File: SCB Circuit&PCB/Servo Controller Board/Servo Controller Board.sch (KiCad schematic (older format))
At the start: 2 parts

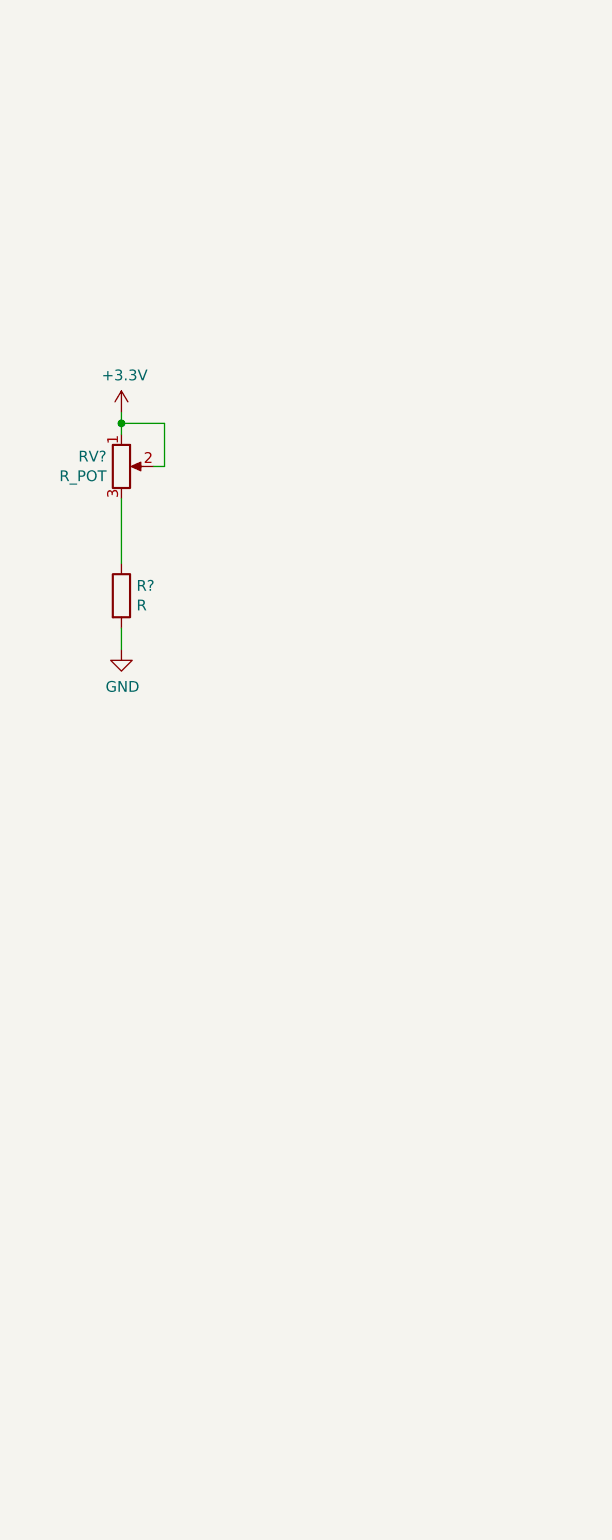
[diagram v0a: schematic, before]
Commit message: Added external interrupt for timer enable/disable
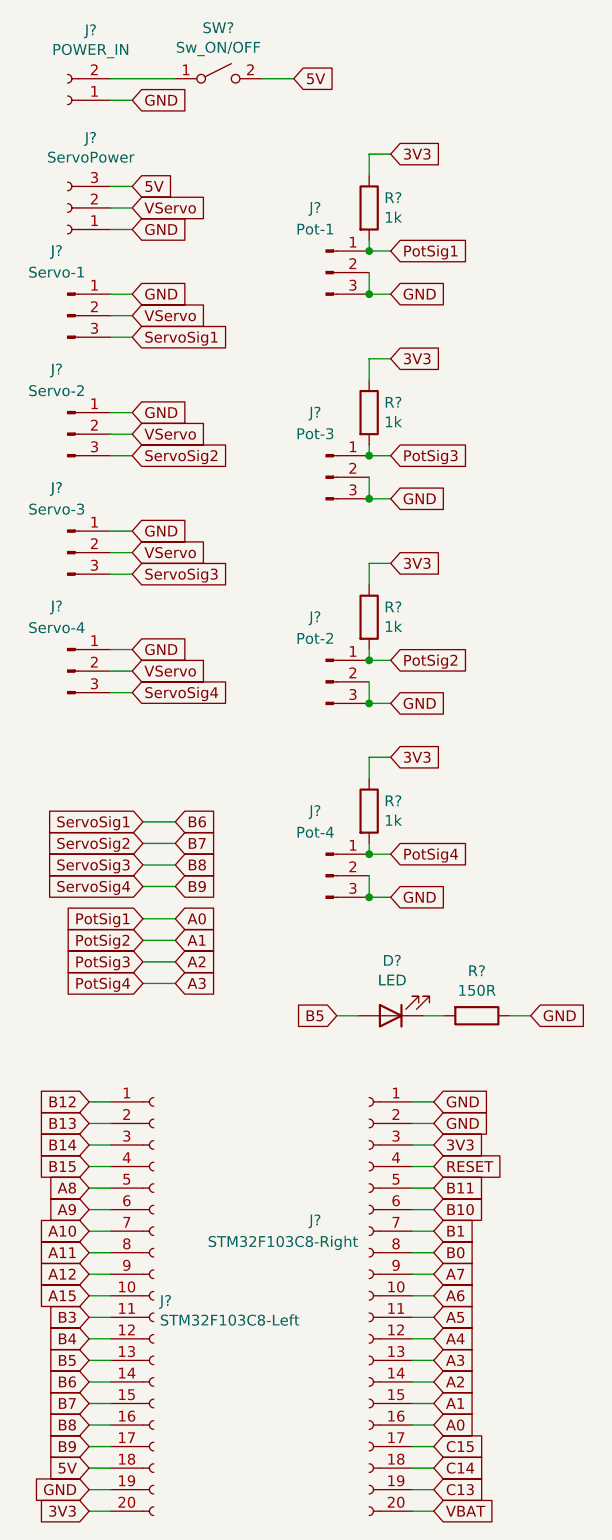
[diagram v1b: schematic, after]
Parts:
- removed R?: R, symbol Device:R
- removed RV?: R_POT, symbol Device:R_POT
- added D?: LED, symbol Device:LED
- added J?: STM32F103C8-Left, symbol Connector:Conn_01x20_Female
- added J?: STM32F103C8-Right, symbol Connector:Conn_01x20_Female
- added J?: POWER_IN, symbol Connector:Conn_01x02_Female
- added J?: Servo-2, symbol Connector:Conn_01x03_Male
- added J?: Servo-1, symbol Connector:Conn_01x03_Male
- added J?: Servo-3, symbol Connector:Conn_01x03_Male
- added J?: Servo-4, symbol Connector:Conn_01x03_Male
- added J?: Pot-1, symbol Connector:Conn_01x03_Male
- added J?: Pot-3, symbol Connector:Conn_01x03_Male
- added J?: Pot-2, symbol Connector:Conn_01x03_Male
- added J?: Pot-4, symbol Connector:Conn_01x03_Male
- added J?: ServoPower, symbol Connector:Conn_01x03_Female
- added R? (x4): 1k, symbol Device:R
- added R?: 150R, symbol Device:R
- added SW?: Sw_ON/OFF, symbol Switch:SW_SPST
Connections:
- net GND: now also J?.1 (Pin_1), J?.1 (Pin_1), J?.1 (Pin_1), J?.1 (Pin_1), J?.1 (Pin_1), J?.1 (Pin_1), J?.1 (Pin_1), J?.19 (Pin_19), J?.2 (Pin_2), J?.2 (Pin_2), J?.2 (Pin_2), J?.2 (Pin_2), J?.2 (Pin_2), J?.3 (Pin_3), J?.3 (Pin_3), J?.3 (Pin_3), J?.3 (Pin_3), R?.1
- new net: J?.2 (Pin_2), SW?.1 (A)
- new net: D?.1 (K), R?.2
- new net 3V3: J?.20 (Pin_20), J?.3 (Pin_3), R?.1, R?.1, R?.1, R?.1
- new net 5V: J?.18 (Pin_18), J?.3 (Pin_3), SW?.2 (B)
- new net A0: J?.1 (Pin_1), J?.16 (Pin_16), R?.2
- new net A1: J?.1 (Pin_1), J?.15 (Pin_15), R?.2
- new net A10: J?.7 (Pin_7)
- new net A11: J?.8 (Pin_8)
- new net A12: J?.9 (Pin_9)
- new net A15: J?.10 (Pin_10)
- new net A2: J?.1 (Pin_1), J?.14 (Pin_14), R?.2
- new net A3: J?.1 (Pin_1), J?.13 (Pin_13), R?.2
- new net A4: J?.12 (Pin_12)
- new net A5: J?.11 (Pin_11)
- new net A6: J?.10 (Pin_10)
- new net A7: J?.9 (Pin_9)
- new net A8: J?.5 (Pin_5)
- new net A9: J?.6 (Pin_6)
- new net B0: J?.8 (Pin_8)
- new net B1: J?.7 (Pin_7)
- new net B10: J?.6 (Pin_6)
- new net B11: J?.5 (Pin_5)
- new net B12: J?.1 (Pin_1)
- new net B13: J?.2 (Pin_2)
- new net B14: J?.3 (Pin_3)
- new net B15: J?.4 (Pin_4)
- new net B3: J?.11 (Pin_11)
- new net B4: J?.12 (Pin_12)
- new net B5: D?.2 (A), J?.13 (Pin_13)
- new net B6: J?.14 (Pin_14), J?.3 (Pin_3)
- new net B7: J?.15 (Pin_15), J?.3 (Pin_3)
- new net B8: J?.16 (Pin_16), J?.3 (Pin_3)
- new net B9: J?.17 (Pin_17), J?.3 (Pin_3)
- new net C13: J?.19 (Pin_19)
- new net C14: J?.18 (Pin_18)
- new net C15: J?.17 (Pin_17)
- new net RESET: J?.4 (Pin_4)
- new net VBAT: J?.20 (Pin_20)
- new net VServo: J?.2 (Pin_2), J?.2 (Pin_2), J?.2 (Pin_2), J?.2 (Pin_2), J?.2 (Pin_2)
